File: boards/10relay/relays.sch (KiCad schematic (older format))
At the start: 8 parts

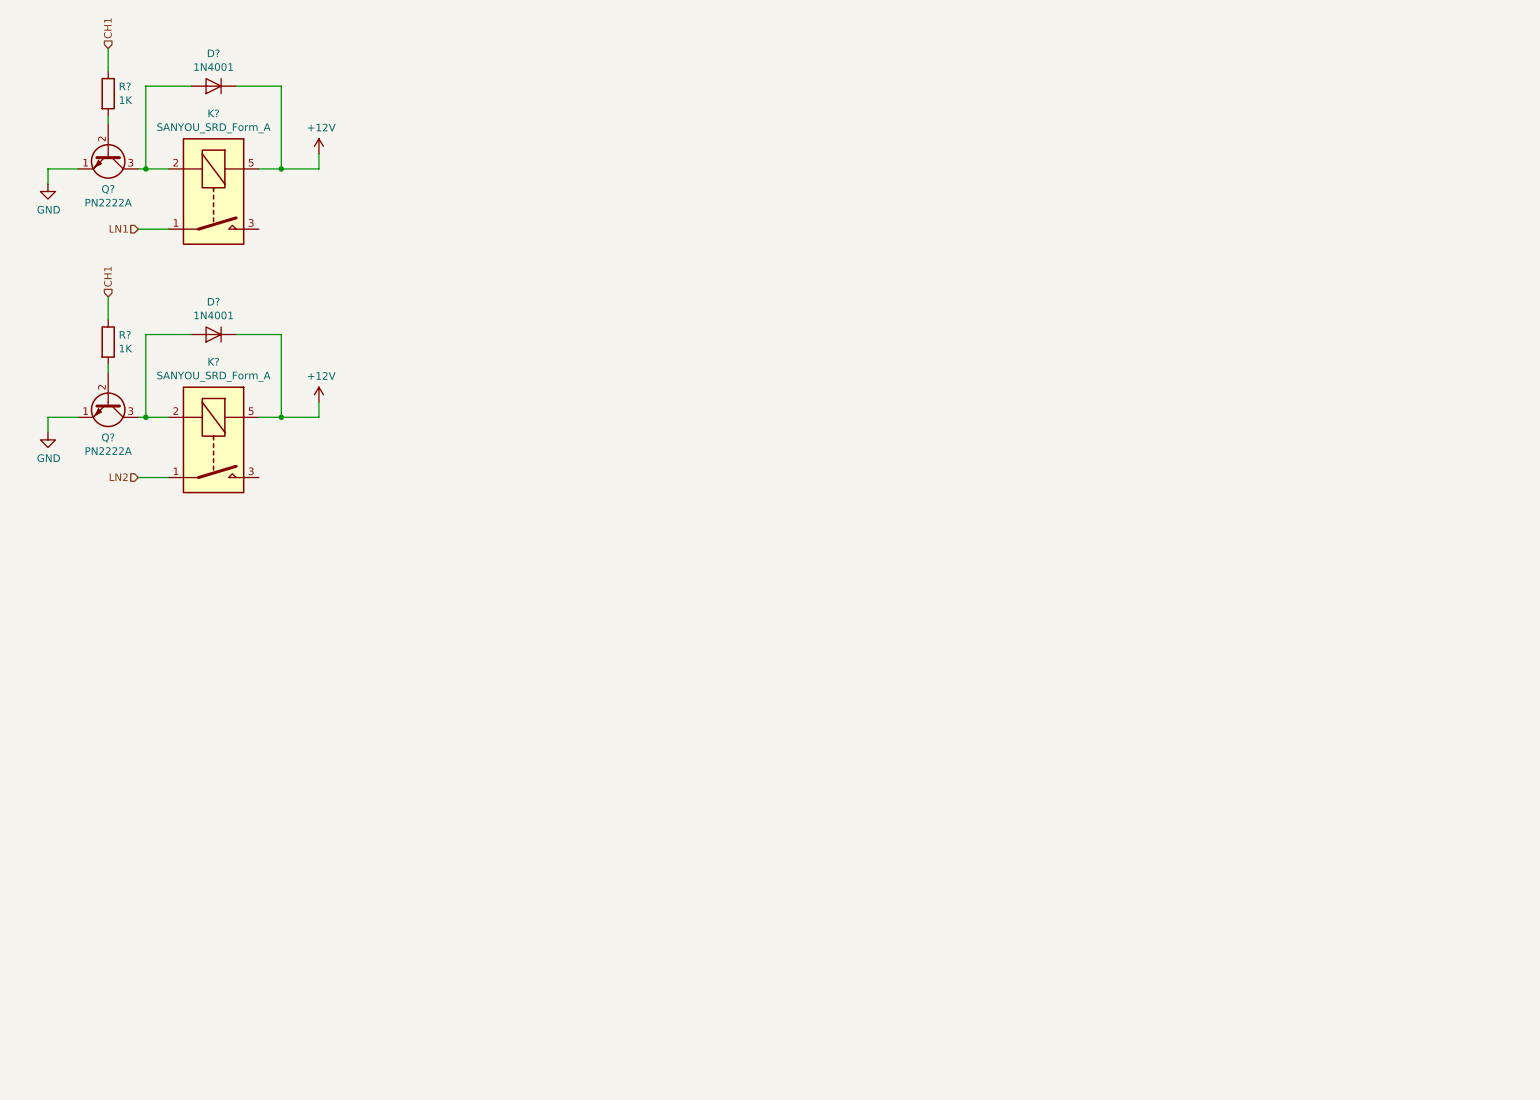
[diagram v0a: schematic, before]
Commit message: Added relay sheet and power sheet
The relay sheet has been added to simplify viewing. It
contains all the relays for all 10 channels. Power sheet
for everything power related such as logic level conversion
and regulators.
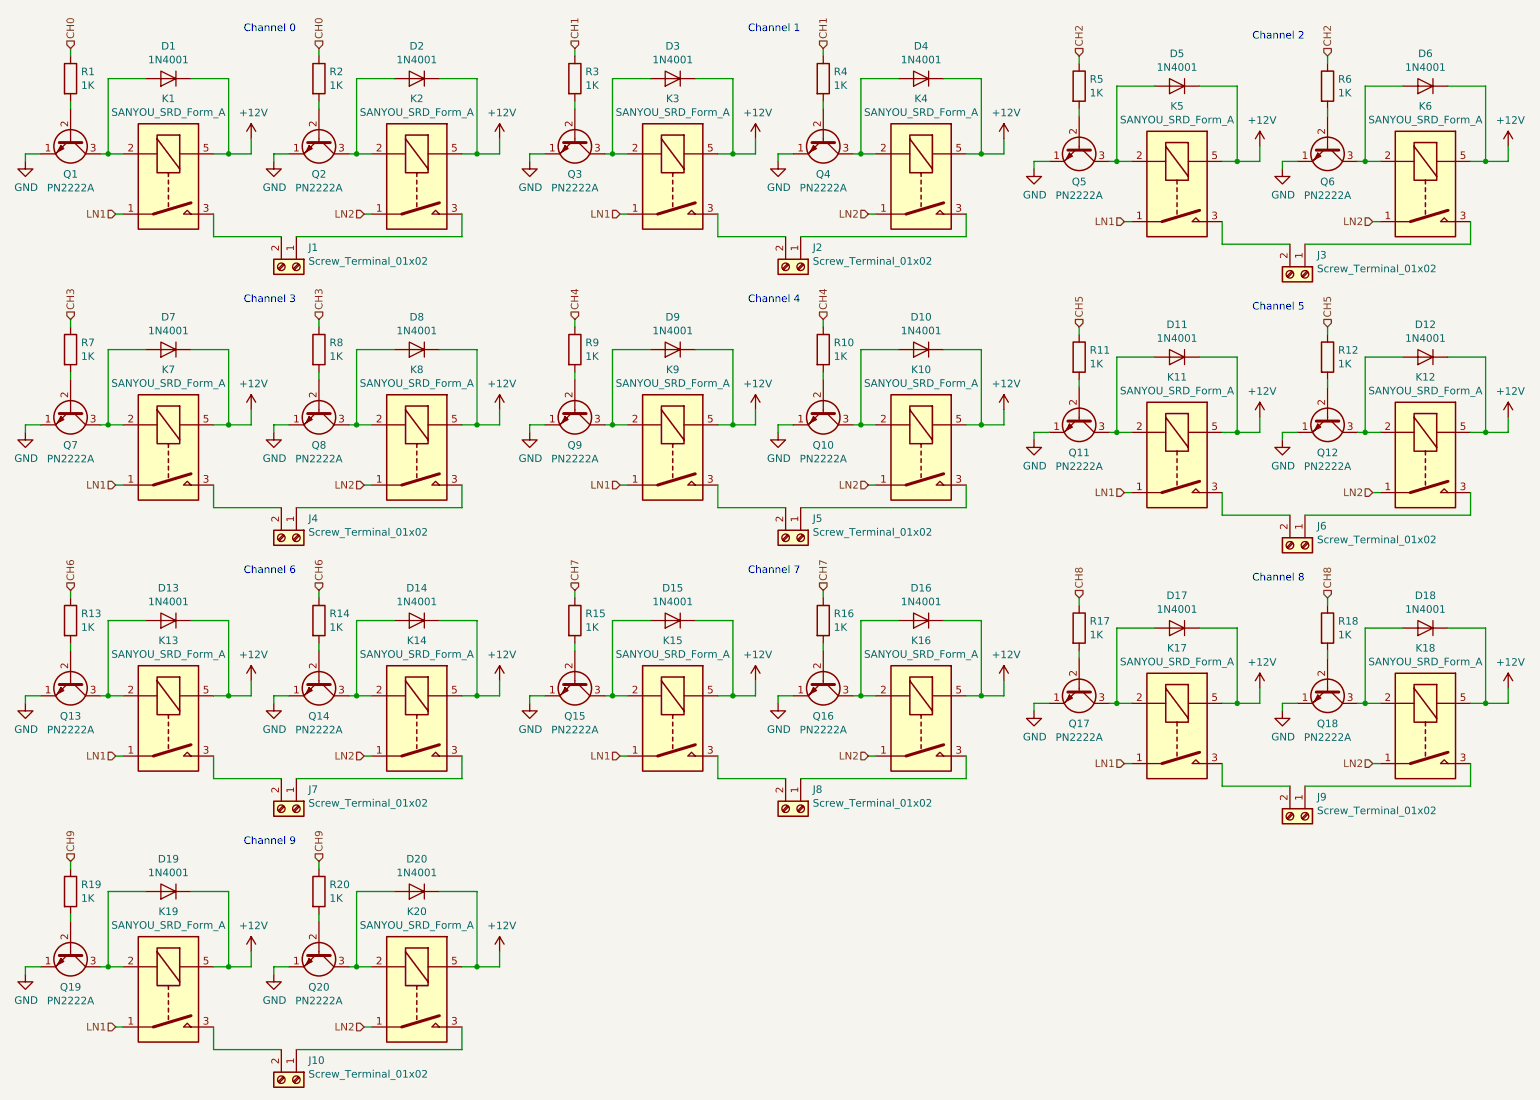
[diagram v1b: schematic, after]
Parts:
- added D10, D11, D12, D13, D14, D15, D16, D17, D18, D19, D20, D3, D4, D5, D6, D7, D8, D9: 1N4001, Diode_THT:D_DO-41_SOD81_P10.16mm_Horizontal, symbol Diode:1N4001
- added J1, J10, J2, J3, J4, J5, J6, J7, J8, J9: Screw_Terminal_01x02, symbol Connector:Screw_Terminal_01x02
- added K10, K11, K12, K13, K14, K15, K16, K17, K18, K19, K20, K3, K4, K5, K6, K7, K8, K9: SANYOU_SRD_Form_A, Relay_THT:Relay_SPST_SANYOU_SRD_Series_Form_A, symbol Relay:SANYOU_SRD_Form_A
- added Q10, Q11, Q12, Q13, Q14, Q15, Q16, Q17, Q18, Q19, Q20, Q3, Q4, Q5, Q6, Q7, Q8, Q9: PN2222A, Package_TO_SOT_THT:TO-92_Inline, symbol Transistor_BJT:PN2222A
- added R10, R11, R12, R13, R14, R15, R16, R17, R18, R19, R20, R3, R4, R5, R6, R7, R8, R9: 1K, symbol Device:R
- gave numbers to parts that had none: 8
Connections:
- net +12V: now also D10.1 (K), D11.1 (K), D12.1 (K), D13.1 (K), D14.1 (K), D15.1 (K), D16.1 (K), D17.1 (K), D18.1 (K), D19.1 (K), D20.1 (K), D3.1 (K), D4.1 (K), D5.1 (K), D6.1 (K), D7.1 (K), D8.1 (K), D9.1 (K), K10.5, K11.5, K12.5, K13.5, K14.5, K15.5, K16.5, K17.5, K18.5, K19.5, K20.5, K3.5, K4.5, K5.5, K6.5, K7.5, K8.5, K9.5
- net CH1: now also R3.1, R4.1; no longer R1.1, R2.1
- net GND: now also Q10.1 (E), Q11.1 (E), Q12.1 (E), Q13.1 (E), Q14.1 (E), Q15.1 (E), Q16.1 (E), Q17.1 (E), Q18.1 (E), Q19.1 (E), Q20.1 (E), Q3.1 (E), Q4.1 (E), Q5.1 (E), Q6.1 (E), Q7.1 (E), Q8.1 (E), Q9.1 (E)
- net LN1: now also K11.1, K13.1, K15.1, K17.1, K19.1, K3.1, K5.1, K7.1, K9.1
- net LN2: now also K10.1, K12.1, K14.1, K16.1, K18.1, K20.1, K4.1, K6.1, K8.1
- net at K1.3: now also J1.2 (Pin_2)
- net at K2.3: now also J1.1 (Pin_1)
- new net: Q3.2 (B), R3.2
- new net: D3.2 (A), K3.2, Q3.3 (C)
- new net: J2.2 (Pin_2), K3.3
- new net: Q4.2 (B), R4.2
- new net: D4.2 (A), K4.2, Q4.3 (C)
- new net: J2.1 (Pin_1), K4.3
- new net: Q5.2 (B), R5.2
- new net: D5.2 (A), K5.2, Q5.3 (C)
- new net: J3.2 (Pin_2), K5.3
- new net: Q6.2 (B), R6.2
- new net: D6.2 (A), K6.2, Q6.3 (C)
- new net: J3.1 (Pin_1), K6.3
- new net: Q7.2 (B), R7.2
- new net: D7.2 (A), K7.2, Q7.3 (C)
- new net: J4.2 (Pin_2), K7.3
- new net: Q8.2 (B), R8.2
- new net: D8.2 (A), K8.2, Q8.3 (C)
- new net: J4.1 (Pin_1), K8.3
- new net: Q9.2 (B), R9.2
- new net: D9.2 (A), K9.2, Q9.3 (C)
- new net: J5.2 (Pin_2), K9.3
- new net: Q10.2 (B), R10.2
- new net: D10.2 (A), K10.2, Q10.3 (C)
- new net: J5.1 (Pin_1), K10.3
- new net: Q11.2 (B), R11.2
- new net: D11.2 (A), K11.2, Q11.3 (C)
- new net: J6.2 (Pin_2), K11.3
- new net: Q12.2 (B), R12.2
- new net: D12.2 (A), K12.2, Q12.3 (C)
- new net: J6.1 (Pin_1), K12.3
- new net: Q13.2 (B), R13.2
- new net: D13.2 (A), K13.2, Q13.3 (C)
- new net: J7.2 (Pin_2), K13.3
- new net: Q14.2 (B), R14.2
- new net: D14.2 (A), K14.2, Q14.3 (C)
- new net: J7.1 (Pin_1), K14.3
- new net: Q15.2 (B), R15.2
- new net: D15.2 (A), K15.2, Q15.3 (C)
- new net: J8.2 (Pin_2), K15.3
- new net: Q16.2 (B), R16.2
- new net: D16.2 (A), K16.2, Q16.3 (C)
- new net: J8.1 (Pin_1), K16.3
- new net: Q17.2 (B), R17.2
- new net: D17.2 (A), K17.2, Q17.3 (C)
- new net: J9.2 (Pin_2), K17.3
- new net: Q18.2 (B), R18.2
- new net: D18.2 (A), K18.2, Q18.3 (C)
- new net: J9.1 (Pin_1), K18.3
- new net: Q19.2 (B), R19.2
- new net: D19.2 (A), K19.2, Q19.3 (C)
- new net: J10.2 (Pin_2), K19.3
- new net: Q20.2 (B), R20.2
- new net: D20.2 (A), K20.2, Q20.3 (C)
- new net: J10.1 (Pin_1), K20.3
- new net CH0: R1.1, R2.1
- new net CH2: R5.1, R6.1
- new net CH3: R7.1, R8.1
- new net CH4: R10.1, R9.1
- new net CH5: R11.1, R12.1
- new net CH6: R13.1, R14.1
- new net CH7: R15.1, R16.1
- new net CH8: R17.1, R18.1
- new net CH9: R19.1, R20.1
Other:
- note added: "Channel 0"
- note added: "Channel 1"
- note added: "Channel 2"
- note added: "Channel 3"
- note added: "Channel 4"
- note added: "Channel 5"
- note added: "Channel 6"
- note added: "Channel 7"
- note added: "Channel 8"
- note added: "Channel 9"
- moved on the sheet: D1, D2, K1, K2, Q1, Q2, R1, R2
